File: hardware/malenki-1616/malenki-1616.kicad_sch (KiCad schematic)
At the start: 28 parts

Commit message: Capacitor voltage rating
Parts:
- C2, C3, C5, C6, C7: LCSC C19702 -> C2922482
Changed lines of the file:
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@@
       (effects (font (size 1.27 1.27)) hide)
     )
-    (property "LCSC" "C19702" (id 5) (at 63.5 52.07 0)
+    (property "LCSC" "C2922482" (id 5) (at 63.5 52.07 0)
       (effects (font (size 1.27 1.27)) hide)
     )
@@
       (effects (font (size 1.27 1.27)) hide)
     )
-    (property "LCSC" "C19702" (id 5) (at 92.71 52.07 0)
+    (property "LCSC" "C2922482" (id 5) (at 92.71 52.07 0)
       (effects (font (size 1.27 1.27)) hide)
     )
@@
       (effects (font (size 1.27 1.27)) hide)
     )
-    (property "LCSC" "C19702" (id 5) (at 219.71 46.99 0)
+    (property "LCSC" "C2922482" (id 5) (at 219.71 46.99 0)
       (effects (font (size 1.27 1.27)) hide)
     )
@@
       (effects (font (size 1.27 1.27)) hide)
     )
-    (property "LCSC" "C19702" (id 5) (at 217.17 97.79 0)
+    (property "LCSC" "C2922482" (id 5) (at 217.17 97.79 0)
       (effects (font (size 1.27 1.27)) hide)
     )
@@
       (effects (font (size 1.27 1.27)) hide)
     )
-    (property "LCSC" "C19702" (id 5) (at 215.9 147.32 0)
+    (property "LCSC" "C2922482" (id 5) (at 215.9 147.32 0)
       (effects (font (size 1.27 1.27)) hide)
     )
@@
     )
     (path "/00000000-0000-0000-0000-00005cdc3232"
-      (reference "C2") (unit 1) (value "10uF") (footprint "Capacitor_SMD:C_0603_1608Metric")
+      (reference "C2") (unit 1) (value "10uF 25V") (footprint "Capacitor_SMD:C_0603_1608Metric")
     )
     (path "/00000000-0000-0000-0000-00005cdc3533"
-      (reference "C3") (unit 1) (value "10uF") (footprint "Capacitor_SMD:C_0603_1608Metric")
+      (reference "C3") (unit 1) (value "10uF 25V") (footprint "Capacitor_SMD:C_0603_1608Metric")
     )
     (path "/00000000-0000-0000-0000-00005cdc5ad8"
@@
     )
     (path "/00000000-0000-0000-0000-00005cdd5c99"
-      (reference "C5") (unit 1) (value "10uF") (footprint "Capacitor_SMD:C_0603_1608Metric")
+      (reference "C5") (unit 1) (value "10uF 25V") (footprint "Capacitor_SMD:C_0603_1608Metric")
     )
     (path "/00000000-0000-0000-0000-00005e3b803a"
-      (reference "C6") (unit 1) (value "10uF") (footprint "Capacitor_SMD:C_0603_1608Metric")
+      (reference "C6") (unit 1) (value "10uF 25V") (footprint "Capacitor_SMD:C_0603_1608Metric")
     )
     (path "/00000000-0000-0000-0000-00005e3c96fb"
-      (reference "C7") (unit 1) (value "10uF") (footprint "Capacitor_SMD:C_0603_1608Metric")
+      (reference "C7") (unit 1) (value "10uF 25V") (footprint "Capacitor_SMD:C_0603_1608Metric")
     )
     (path "/00000000-0000-0000-0000-00005cdd2ed4"

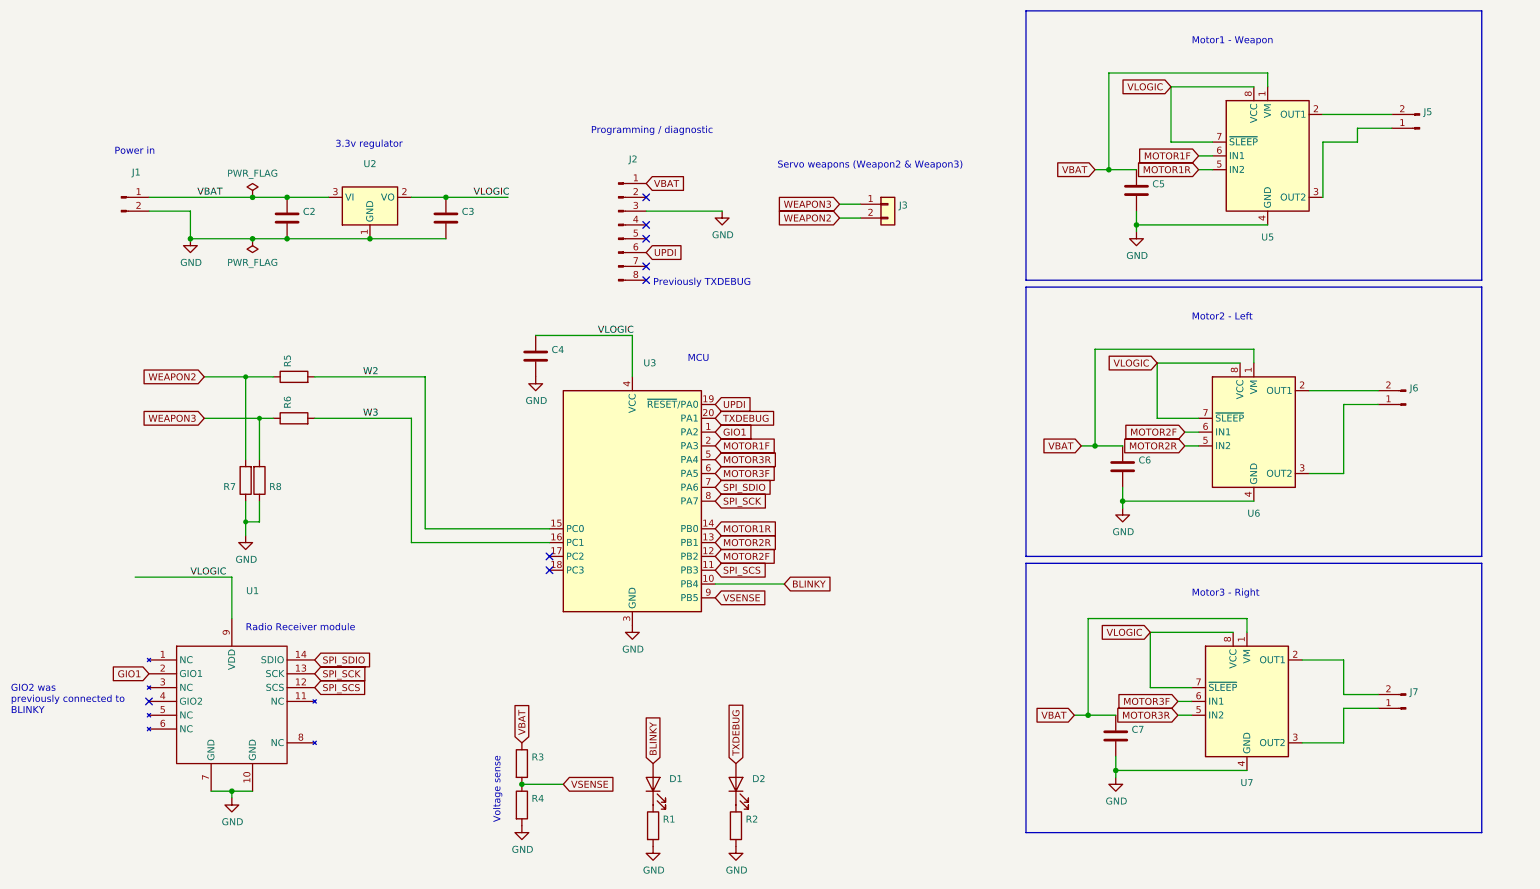
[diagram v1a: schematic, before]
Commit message: Malenki 1616 - component swap on voltage reg
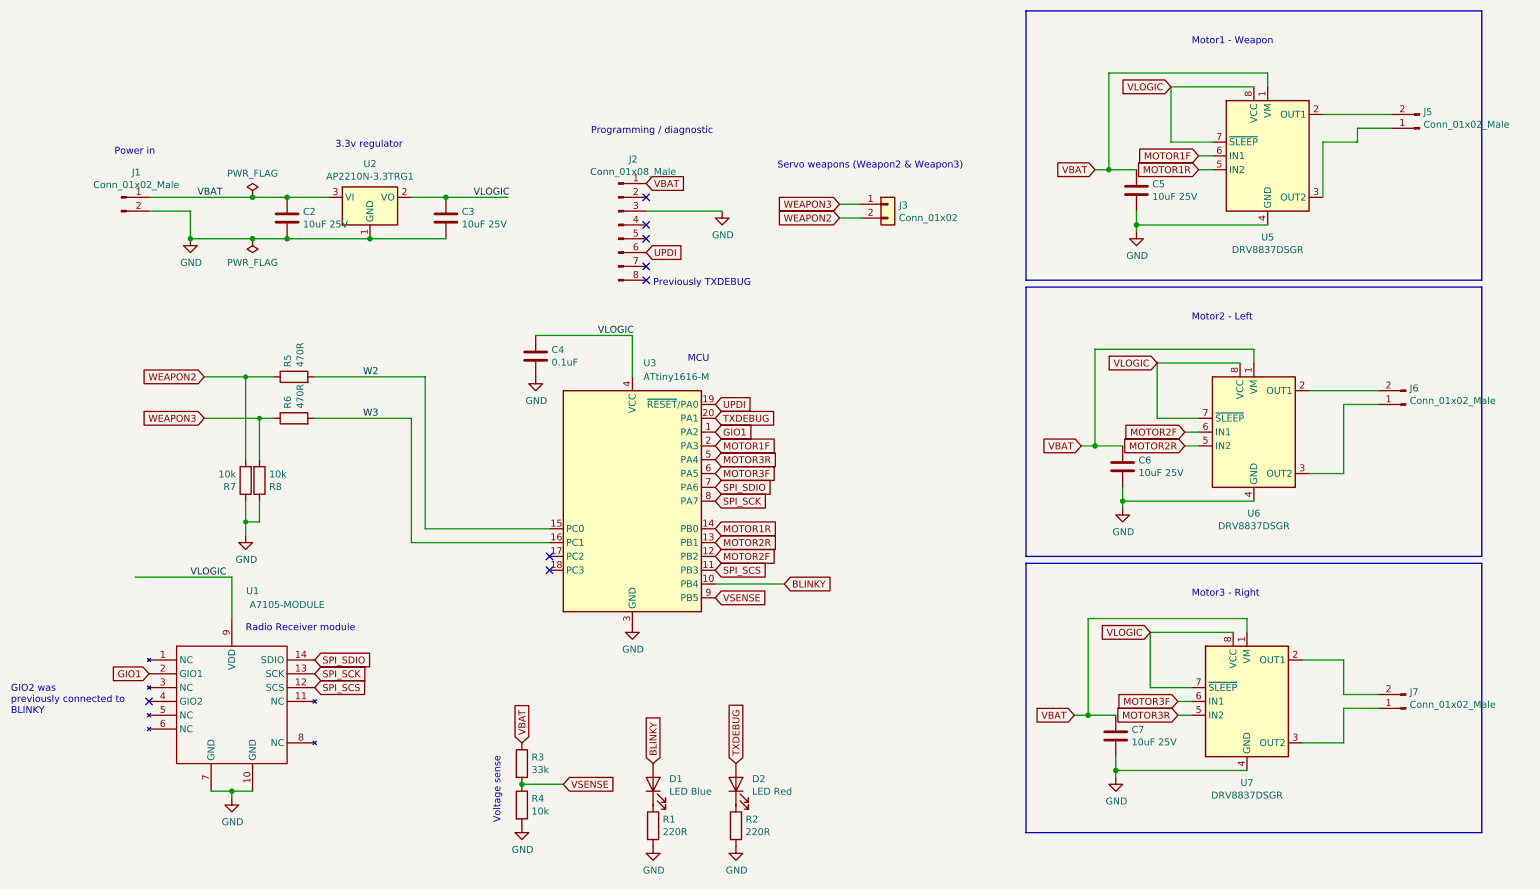
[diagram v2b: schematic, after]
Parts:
- C2, C3, C5, C6, C7: value (none) -> 10uF 25V; footprint (none) -> Capacitor_SMD:C_0603_1608Metric; LCSC C2922482 -> C96446
- C4: value (none) -> 0.1uF; footprint (none) -> Capacitor_SMD:C_0603_1608Metric
- D1: value (none) -> LED Blue; footprint (none) -> LED_SMD:LED_0805_2012Metric_Pad1.15x1.40mm_HandSolder
- D2: value (none) -> LED Red; footprint (none) -> LED_SMD:LED_0805_2012Metric_Pad1.15x1.40mm_HandSolder
- J1, J5, J6, J7: value (none) -> Conn_01x02_Male; footprint (none) -> malenki-nano:PinHeader_1x02_P2.54mm_BIG1
- J2: value (none) -> Conn_01x08_Male; footprint (none) -> malenki-nano:SOIC_clipProgSmall
- J3: value (none) -> Conn_01x02; footprint (none) -> malenki-nano:wirepad_2
- R1, R2: value (none) -> 220R; footprint (none) -> Resistor_SMD:R_0603_1608Metric
- R3: value (none) -> 33k; footprint (none) -> Resistor_SMD:R_0603_1608Metric
- R4: value (none) -> 10k; footprint (none) -> Resistor_SMD:R_0603_1608Metric
- R5, R6: value (none) -> 470R; footprint (none) -> Resistor_SMD:R_0402_1005Metric
- R7, R8: value (none) -> 10k; footprint (none) -> Resistor_SMD:R_0402_1005Metric
- U1: value (none) -> A7105-MODULE; footprint (none) -> malenki-nano:A7105-module
- U2: value (none) -> AP2210N-3.3TRG1; footprint (none) -> Package_TO_SOT_SMD:SOT-23; Partnum C211659 -> C155508
- U3: value (none) -> ATtiny1616-M; footprint (none) -> Package_DFN_QFN:VQFN-20-1EP_3x3mm_P0.4mm_EP1.7x1.7mm
- U5, U6, U7: value (none) -> DRV8837DSGR; footprint (none) -> malenki-nano:WSON-8-1EP_2x2mm_P0.5mm_HAND1

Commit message: Updates to old stuff
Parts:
- U2: LCSC C211659 -> C155508; Partnum C155508 -> (none)
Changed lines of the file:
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@@
       (effects (font (size 1.27 1.27)) hide)
     )
-    (property "Partnum" "C155508" (id 4) (at 78.74 44.45 0)
+    (property "Partnum" "" (id 4) (at 78.74 44.45 0)
       (effects (font (size 1.27 1.27)) hide)
     )
-    (property "LCSC" "C211659" (id 5) (at 78.74 44.45 0)
+    (property "LCSC" "C155508" (id 5) (at 78.74 44.45 0)
       (effects (font (size 1.27 1.27)) hide)
     )
